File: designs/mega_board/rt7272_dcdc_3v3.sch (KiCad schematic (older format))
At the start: 14 parts, among them U2 RT7272

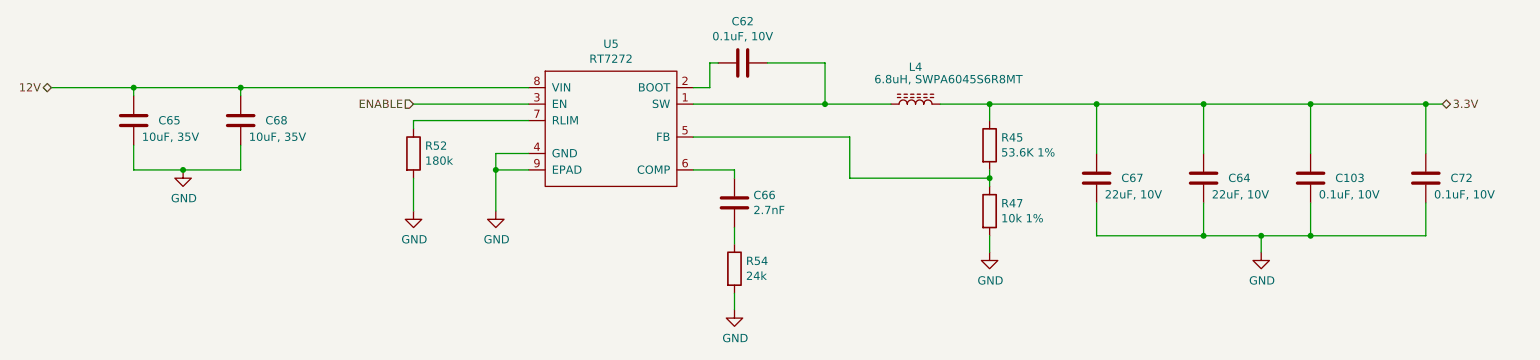
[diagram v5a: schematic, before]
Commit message: Add BOM definition to all resistors
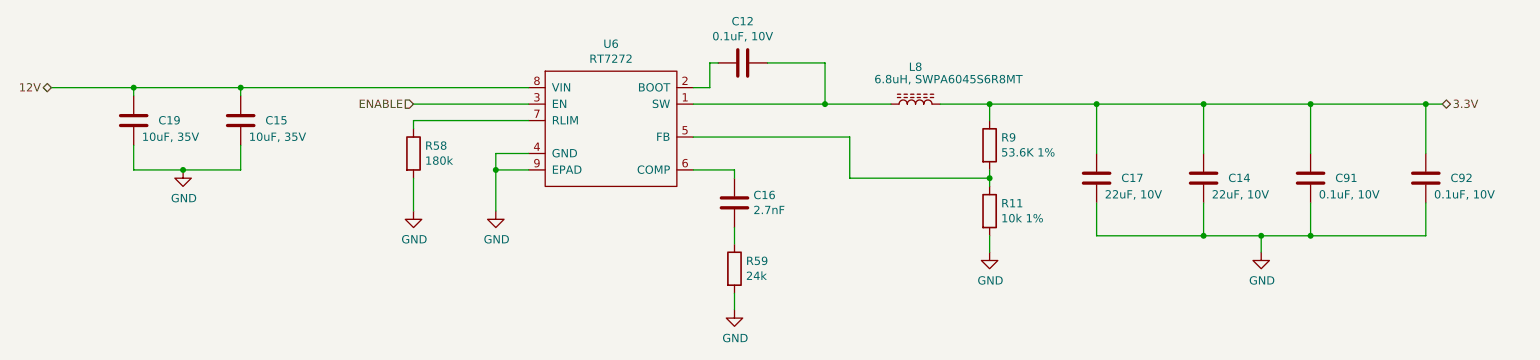
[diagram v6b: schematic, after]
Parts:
- R14: Manufacturer (none) -> Panasonic Electronic Components; Manufacturer PN (none) -> ERJ-2RKF5362X; Supplier (none) -> DigiKey; Supplier PN (none) -> P53.6KLDKR-ND
- R15: Manufacturer (none) -> Panasonic Electronic Components; Manufacturer PN (none) -> ERJ-PA2F1002X; Supplier (none) -> DigiKey; Supplier PN (none) -> P17230DKR-ND
- R19: Manufacturer (none) -> Panasonic Electronic Components; Manufacturer PN (none) -> ERJ-PA2F1803X; Supplier (none) -> DigiKey; Supplier PN (none) -> P124450DKR-ND
- R37: Manufacturer (none) -> Panasonic Electronic Components; Manufacturer PN (none) -> ERJ-PA2F2402X; Supplier (none) -> DigiKey; Supplier PN (none) -> P124459DKR-ND
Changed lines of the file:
@@
 $Descr A4 11693 8268
 encoding utf-8
-Sheet 5 14
+Sheet 6 14
 Title ""
 Date ""
@@
 AR Path="/5D0328DE/5D42E225/5D42D1B4" Ref="U6"  Part="1"
 AR Path="/5D42D1B4" Ref="U?"  Part="1"
-F 0 "U5" H 5600 4015 50  0000 C CNN
+F 0 "U6" H 5600 4015 50  0000 C CNN
 F 1 "RT7272" H 5600 3924 50  0000 C CNN
 F 2 "LibreRouter_MegaBoard:RT8250-SOP8" H 5600 3500 50  0001 C CNN
@@
 AR Path="/5D0328DE/5D42CD47/5D42D229" Ref="C29"  Part="1"
 AR Path="/5D0328DE/5D42E225/5D42D229" Ref="C15"  Part="1"
-F 0 "C68" H 3500 3450 50  0000 L CNN
+F 0 "C15" H 3500 3450 50  0000 L CNN
 F 1 "10uF, 35V" H 3400 3350 50  0000 L CNN
 F 2 "LibreRouter_MegaBoard:C0805" H 3388 3300 50  0001 C CNN
@@
 AR Path="/5D0328DE/5D42CD47/5D42D2DE" Ref="R19"  Part="1"
 AR Path="/5D0328DE/5D42E225/5D42D2DE" Ref="R58"  Part="1"
-F 0 "R52" H 4470 3696 50  0000 L CNN
+F 0 "R58" H 4470 3696 50  0000 L CNN
 F 1 "180k" H 4470 3605 50  0000 L CNN
 F 2 "LibreRouter_MegaBoard:R0402" V 4330 3650 50  0001 C CNN
 F 3 "~" H 4400 3650 50  0001 C CNN
+F 4 "Panasonic Electronic Components" H 4400 3650 50  0001 C CNN "Manufacturer"
+F 5 "ERJ-PA2F1803X" H 4400 3650 50  0001 C CNN "Manufacturer PN"
+F 6 "DigiKey" H 4400 3650 50  0001 C CNN "Supplier"
+F 7 "P124450DKR-ND" H 4400 3650 50  0001 C CNN "Supplier PN"
 	1    4400 3650
 	1    0    0    -1
@@
 AR Path="/5D0328DE/5D42CD47/5D42D3B9" Ref="L2"  Part="1"
 AR Path="/5D0328DE/5D42E225/5D42D3B9" Ref="L8"  Part="1"
-F 0 "L4" V 7675 3350 50  0000 C CNN
+F 0 "L8" V 7675 3350 50  0000 C CNN
 F 1 "6.8uH, SWPA6045S6R8MT" V 7600 3150 50  0000 C CNN
 F 2 "LibreRouter_MegaBoard:SWPA6028S" H 7450 3350 50  0001 C CNN
@@
 AR Path="/5D0328DE/5D42CD47/5D42D488" Ref="C13"  Part="1"
 AR Path="/5D0328DE/5D42E225/5D42D488" Ref="C12"  Part="1"
-F 0 "C62" V 6148 3100 50  0000 C CNN
+F 0 "C12" V 6148 3100 50  0000 C CNN
 F 1 "0.1uF, 10V" V 6239 3100 50  0000 C CNN
 F 2 "LibreRouter_MegaBoard:C0402" H 6438 2950 50  0001 C CNN
@@
 AR Path="/5D0328DE/5D42CD47/5D42D571" Ref="R14"  Part="1"
 AR Path="/5D0328DE/5D42E225/5D42D571" Ref="R9"  Part="1"
-F 0 "R45" H 7970 3646 50  0000 L CNN
+F 0 "R9" H 7970 3646 50  0000 L CNN
 F 1 "53.6K 1%" H 7970 3555 50  0000 L CNN
 F 2 "LibreRouter_MegaBoard:R0402" V 7830 3600 50  0001 C CNN
 F 3 "~" H 7900 3600 50  0001 C CNN
+F 4 "Panasonic Electronic Components" H 7900 3600 50  0001 C CNN "Manufacturer"
+F 5 "ERJ-2RKF5362X" H 7900 3600 50  0001 C CNN "Manufacturer PN"
+F 6 "DigiKey" H 7900 3600 50  0001 C CNN "Supplier"
+F 7 "P53.6KLDKR-ND" H 7900 3600 50  0001 C CNN "Supplier PN"
 	1    7900 3600
 	1    0    0    -1
@@
 AR Path="/5D0328DE/5D42CD47/5D42D5CB" Ref="R15"  Part="1"
 AR Path="/5D0328DE/5D42E225/5D42D5CB" Ref="R11"  Part="1"
-F 0 "R47" H 7970 4046 50  0000 L CNN
+F 0 "R11" H 7970 4046 50  0000 L CNN
 F 1 "10k 1%" H 7970 3955 50  0000 L CNN
 F 2 "LibreRouter_MegaBoard:R0402" V 7830 4000 50  0001 C CNN
 F 3 "~" H 7900 4000 50  0001 C CNN
+F 4 "Panasonic Electronic Components" H 7900 4000 50  0001 C CNN "Manufacturer"
+F 5 "ERJ-PA2F1002X" H 7900 4000 50  0001 C CNN "Manufacturer PN"
+F 6 "DigiKey" H 7900 4000 50  0001 C CNN "Supplier"
+F 7 "P17230DKR-ND" H 7900 4000 50  0001 C CNN "Supplier PN"
 	1    7900 4000
 	1    0    0    -1
@@
 AR Path="/5D0328DE/5D42CD47/5D42D605" Ref="R37"  Part="1"
 AR Path="/5D0328DE/5D42E225/5D42D605" Ref="R59"  Part="1"
-F 0 "R54" H 6420 4396 50  0000 L CNN
+F 0 "R59" H 6420 4396 50  0000 L CNN
 F 1 "24k" H 6420 4305 50  0000 L CNN
 F 2 "LibreRouter_MegaBoard:R0402" V 6280 4350 50  0001 C CNN
 F 3 "~" H 6350 4350 50  0001 C CNN
+F 4 "Panasonic Electronic Components" H 6350 4350 50  0001 C CNN "Manufacturer"
+F 5 "ERJ-PA2F2402X" H 6350 4350 50  0001 C CNN "Manufacturer PN"
+F 6 "DigiKey" H 6350 4350 50  0001 C CNN "Supplier"
+F 7 "P124459DKR-ND" H 6350 4350 50  0001 C CNN "Supplier PN"
 	1    6350 4350
 	1    0    0    -1
@@
 AR Path="/5D0328DE/5D42CD47/5D42D659" Ref="C32"  Part="1"
 AR Path="/5D0328DE/5D42E225/5D42D659" Ref="C16"  Part="1"
-F 0 "C66" H 6235 3904 50  0000 R CNN
+F 0 "C16" H 6235 3904 50  0000 R CNN
 F 1 "2.7nF" H 6235 3995 50  0000 R CNN
 F 2 "LibreRouter_MegaBoard:C0402" H 6388 3800 50  0001 C CNN
@@
 AR Path="/5D0328DE/5D42CD47/5D42DAC0" Ref="C38"  Part="1"
 AR Path="/5D0328DE/5D42E225/5D42DAC0" Ref="C17"  Part="1"
-F 0 "C67" H 8400 3800 50  0000 R CNN
+F 0 "C17" H 8400 3800 50  0000 R CNN
 F 1 "22uF, 10V" H 8500 3900 50  0000 R CNN
 F 2 "LibreRouter_MegaBoard:C0805" H 8588 3650 50  0001 C CNN
@@
 AR Path="/5D0328DE/5D42CD47/5D42DBCD" Ref="C28"  Part="1"
 AR Path="/5D0328DE/5D42E225/5D42DBCD" Ref="C14"  Part="1"
-F 0 "C64" H 9050 3800 50  0000 R CNN
+F 0 "C14" H 9050 3800 50  0000 R CNN
 F 1 "22uF, 10V" H 9150 3900 50  0000 R CNN
 F 2 "LibreRouter_MegaBoard:C0805" H 9238 3650 50  0001 C CNN
@@
 AR Path="/5D0328DE/5D42CD47/5D42DC2B" Ref="C71"  Part="1"
 AR Path="/5D0328DE/5D42E225/5D42DC2B" Ref="C91"  Part="1"
-F 0 "C103" H 9700 3800 50  0000 R CNN
+F 0 "C91" H 9700 3800 50  0000 R CNN
 F 1 "0.1uF, 10V" H 9800 3900 50  0000 R CNN
 F 2 "LibreRouter_MegaBoard:C0402" H 9888 3650 50  0001 C CNN
@@
 AR Path="/5D0328DE/5D42CD47/5D42DCB2" Ref="C72"  Part="1"
 AR Path="/5D0328DE/5D42E225/5D42DCB2" Ref="C92"  Part="1"
-F 0 "C72" H 10400 3800 50  0000 R CNN
+F 0 "C92" H 10400 3800 50  0000 R CNN
 F 1 "0.1uF, 10V" H 10500 3900 50  0000 R CNN
 F 2 "LibreRouter_MegaBoard:C0402" H 10588 3650 50  0001 C CNN
@@
 AR Path="/5D0328DE/5D42CD47/5D42DD90" Ref="#PWR0139"  Part="1"
 AR Path="/5D0328DE/5D42E225/5D42DD90" Ref="#PWR0145"  Part="1"
-F 0 "#PWR0139" H 7900 4000 50  0001 C CNN
+F 0 "#PWR0145" H 7900 4000 50  0001 C CNN
 F 1 "GND" H 7905 4077 50  0000 C CNN
 F 2 "" H 7900 4250 50  0001 C CNN
@@
 AR Path="/5D0328DE/5D42CD47/5D42DDBC" Ref="#PWR0140"  Part="1"
 AR Path="/5D0328DE/5D42E225/5D42DDBC" Ref="#PWR0146"  Part="1"
-F 0 "#PWR0140" H 9550 4000 50  0001 C CNN
+F 0 "#PWR0146" H 9550 4000 50  0001 C CNN
 F 1 "GND" H 9555 4077 50  0000 C CNN
 F 2 "" H 9550 4250 50  0001 C CNN
@@
 AR Path="/5D0328DE/5D42CD47/5D42FF27" Ref="#PWR0141"  Part="1"
 AR Path="/5D0328DE/5D42E225/5D42FF27" Ref="#PWR0147"  Part="1"
-F 0 "#PWR0141" H 6350 4350 50  0001 C CNN
+F 0 "#PWR0147" H 6350 4350 50  0001 C CNN
 F 1 "GND" H 6355 4427 50  0000 C CNN
 F 2 "" H 6350 4600 50  0001 C CNN
@@
 AR Path="/5D0328DE/5D42CD47/5D43058C" Ref="C36"  Part="1"
 AR Path="/5D0328DE/5D42E225/5D43058C" Ref="C19"  Part="1"
-F 0 "C65" H 2850 3450 50  0000 L CNN
+F 0 "C19" H 2850 3450 50  0000 L CNN
 F 1 "10uF, 35V" H 2750 3350 50  0000 L CNN
 F 2 "LibreRouter_MegaBoard:C0805" H 2738 3300 50  0001 C CNN
@@
 AR Path="/5D0328DE/5D42CD47/5D4322E2" Ref="#PWR0142"  Part="1"
 AR Path="/5D0328DE/5D42E225/5D4322E2" Ref="#PWR0148"  Part="1"
-F 0 "#PWR0142" H 3000 3500 50  0001 C CNN
+F 0 "#PWR0148" H 3000 3500 50  0001 C CNN
 F 1 "GND" H 3005 3577 50  0000 C CNN
 F 2 "" H 3000 3750 50  0001 C CNN
@@
 AR Path="/5D0328DE/5D42CD47/5D4323C5" Ref="#PWR0143"  Part="1"
 AR Path="/5D0328DE/5D42E225/5D4323C5" Ref="#PWR0149"  Part="1"
-F 0 "#PWR0143" H 4400 3750 50  0001 C CNN
+F 0 "#PWR0149" H 4400 3750 50  0001 C CNN
 F 1 "GND" H 4405 3827 50  0000 C CNN
 F 2 "" H 4400 4000 50  0001 C CNN
@@
 AR Path="/5D0328DE/5D42CD47/5D4323EC" Ref="#PWR0144"  Part="1"
 AR Path="/5D0328DE/5D42E225/5D4323EC" Ref="#PWR0150"  Part="1"
-F 0 "#PWR0144" H 4900 3750 50  0001 C CNN
+F 0 "#PWR0150" H 4900 3750 50  0001 C CNN
 F 1 "GND" H 4905 3827 50  0000 C CNN
 F 2 "" H 4900 4000 50  0001 C CNN

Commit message: Add BOM definition for components. We need more iformation for all the components that are not defined.
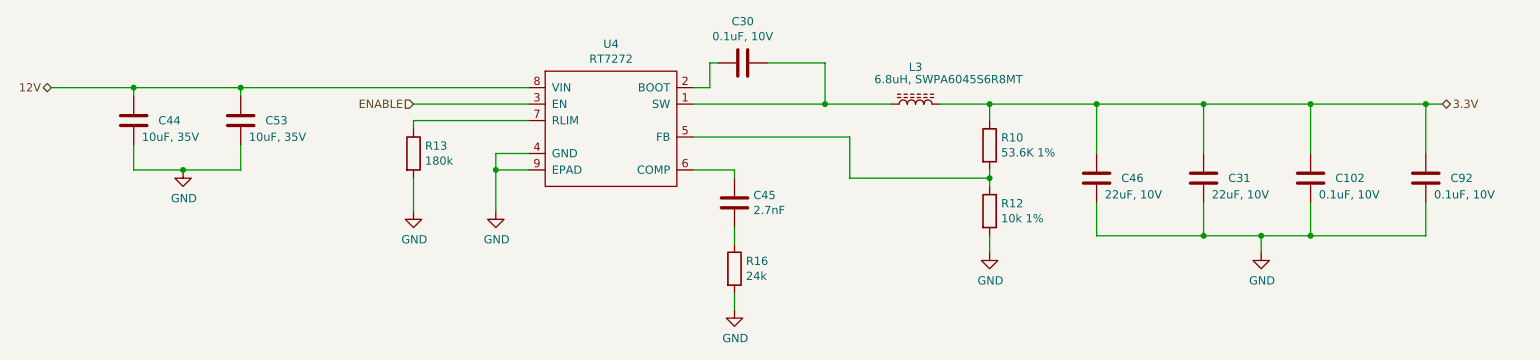
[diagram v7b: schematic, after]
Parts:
- L2: Manufacturer (none) -> Abracon LLC; Manufacturer PN (none) -> ASPI-6045S-6R8M-T; Supplier (none) -> DigiKey; Supplier PN (none) -> 535-13046-6-ND
- U2: Manufacturer (none) -> Richtek USA Inc.; Manufacturer PN (none) -> RT7272AGSP; Supplier (none) -> DigiKey; Supplier PN (none) -> RT7272AGSPDKR-ND
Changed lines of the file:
@@
 AR Path="/5D0328DE/5D42E225/5D42D1B4" Ref="U6"  Part="1"
 AR Path="/5D42D1B4" Ref="U?"  Part="1"
-F 0 "U6" H 5600 4015 50  0000 C CNN
+F 0 "U4" H 5600 4015 50  0000 C CNN
 F 1 "RT7272" H 5600 3924 50  0000 C CNN
 F 2 "LibreRouter_MegaBoard:RT8250-SOP8" H 5600 3500 50  0001 C CNN
 F 3 "" H 5600 3500 50  0001 C CNN
+F 4 "Richtek USA Inc." H 5600 3500 50  0001 C CNN "Manufacturer"
+F 5 "RT7272AGSP" H 5600 3500 50  0001 C CNN "Manufacturer PN"
+F 6 "DigiKey" H 5600 3500 50  0001 C CNN "Supplier"
+F 7 "RT7272AGSPDKR-ND" H 5600 3500 50  0001 C CNN "Supplier PN"
 	1    5600 3500
 	1    0    0    -1
@@
 AR Path="/5D0328DE/5D42CD47/5D42D229" Ref="C29"  Part="1"
 AR Path="/5D0328DE/5D42E225/5D42D229" Ref="C15"  Part="1"
-F 0 "C15" H 3500 3450 50  0000 L CNN
+F 0 "C53" H 3500 3450 50  0000 L CNN
 F 1 "10uF, 35V" H 3400 3350 50  0000 L CNN
 F 2 "LibreRouter_MegaBoard:C0805" H 3388 3300 50  0001 C CNN
@@
 AR Path="/5D0328DE/5D42CD47/5D42D2DE" Ref="R19"  Part="1"
 AR Path="/5D0328DE/5D42E225/5D42D2DE" Ref="R58"  Part="1"
-F 0 "R58" H 4470 3696 50  0000 L CNN
+F 0 "R13" H 4470 3696 50  0000 L CNN
 F 1 "180k" H 4470 3605 50  0000 L CNN
 F 2 "LibreRouter_MegaBoard:R0402" V 4330 3650 50  0001 C CNN
@@
 AR Path="/5D0328DE/5D42CD47/5D42D3B9" Ref="L2"  Part="1"
 AR Path="/5D0328DE/5D42E225/5D42D3B9" Ref="L8"  Part="1"
-F 0 "L8" V 7675 3350 50  0000 C CNN
+F 0 "L3" V 7675 3350 50  0000 C CNN
 F 1 "6.8uH, SWPA6045S6R8MT" V 7600 3150 50  0000 C CNN
 F 2 "LibreRouter_MegaBoard:SWPA6028S" H 7450 3350 50  0001 C CNN
 F 3 "~" H 7450 3350 50  0001 C CNN
+F 4 "Abracon LLC" H 7450 3350 50  0001 C CNN "Manufacturer"
+F 5 "ASPI-6045S-6R8M-T" H 7450 3350 50  0001 C CNN "Manufacturer PN"
+F 6 "DigiKey" H 7450 3350 50  0001 C CNN "Supplier"
+F 7 "535-13046-6-ND" H 7450 3350 50  0001 C CNN "Supplier PN"
 	1    7450 3350
 	0    -1   -1   0
@@
 AR Path="/5D0328DE/5D42CD47/5D42D488" Ref="C13"  Part="1"
 AR Path="/5D0328DE/5D42E225/5D42D488" Ref="C12"  Part="1"
-F 0 "C12" V 6148 3100 50  0000 C CNN
+F 0 "C30" V 6148 3100 50  0000 C CNN
 F 1 "0.1uF, 10V" V 6239 3100 50  0000 C CNN
 F 2 "LibreRouter_MegaBoard:C0402" H 6438 2950 50  0001 C CNN
@@
 AR Path="/5D0328DE/5D42CD47/5D42D571" Ref="R14"  Part="1"
 AR Path="/5D0328DE/5D42E225/5D42D571" Ref="R9"  Part="1"
-F 0 "R9" H 7970 3646 50  0000 L CNN
+F 0 "R10" H 7970 3646 50  0000 L CNN
 F 1 "53.6K 1%" H 7970 3555 50  0000 L CNN
 F 2 "LibreRouter_MegaBoard:R0402" V 7830 3600 50  0001 C CNN
@@
 AR Path="/5D0328DE/5D42CD47/5D42D5CB" Ref="R15"  Part="1"
 AR Path="/5D0328DE/5D42E225/5D42D5CB" Ref="R11"  Part="1"
-F 0 "R11" H 7970 4046 50  0000 L CNN
+F 0 "R12" H 7970 4046 50  0000 L CNN
 F 1 "10k 1%" H 7970 3955 50  0000 L CNN
 F 2 "LibreRouter_MegaBoard:R0402" V 7830 4000 50  0001 C CNN
@@
 AR Path="/5D0328DE/5D42CD47/5D42D605" Ref="R37"  Part="1"
 AR Path="/5D0328DE/5D42E225/5D42D605" Ref="R59"  Part="1"
-F 0 "R59" H 6420 4396 50  0000 L CNN
+F 0 "R16" H 6420 4396 50  0000 L CNN
 F 1 "24k" H 6420 4305 50  0000 L CNN
 F 2 "LibreRouter_MegaBoard:R0402" V 6280 4350 50  0001 C CNN
@@
 AR Path="/5D0328DE/5D42CD47/5D42D659" Ref="C32"  Part="1"
 AR Path="/5D0328DE/5D42E225/5D42D659" Ref="C16"  Part="1"
-F 0 "C16" H 6235 3904 50  0000 R CNN
+F 0 "C45" H 6235 3904 50  0000 R CNN
 F 1 "2.7nF" H 6235 3995 50  0000 R CNN
 F 2 "LibreRouter_MegaBoard:C0402" H 6388 3800 50  0001 C CNN
@@
 AR Path="/5D0328DE/5D42CD47/5D42DAC0" Ref="C38"  Part="1"
 AR Path="/5D0328DE/5D42E225/5D42DAC0" Ref="C17"  Part="1"
-F 0 "C17" H 8400 3800 50  0000 R CNN
+F 0 "C46" H 8400 3800 50  0000 R CNN
 F 1 "22uF, 10V" H 8500 3900 50  0000 R CNN
 F 2 "LibreRouter_MegaBoard:C0805" H 8588 3650 50  0001 C CNN
@@
 AR Path="/5D0328DE/5D42CD47/5D42DBCD" Ref="C28"  Part="1"
 AR Path="/5D0328DE/5D42E225/5D42DBCD" Ref="C14"  Part="1"
-F 0 "C14" H 9050 3800 50  0000 R CNN
+F 0 "C31" H 9050 3800 50  0000 R CNN
 F 1 "22uF, 10V" H 9150 3900 50  0000 R CNN
 F 2 "LibreRouter_MegaBoard:C0805" H 9238 3650 50  0001 C CNN
@@
 AR Path="/5D0328DE/5D42CD47/5D42DC2B" Ref="C71"  Part="1"
 AR Path="/5D0328DE/5D42E225/5D42DC2B" Ref="C91"  Part="1"
-F 0 "C91" H 9700 3800 50  0000 R CNN
+F 0 "C102" H 9700 3800 50  0000 R CNN
 F 1 "0.1uF, 10V" H 9800 3900 50  0000 R CNN
 F 2 "LibreRouter_MegaBoard:C0402" H 9888 3650 50  0001 C CNN
@@
 AR Path="/5D0328DE/5D42CD47/5D43058C" Ref="C36"  Part="1"
 AR Path="/5D0328DE/5D42E225/5D43058C" Ref="C19"  Part="1"
-F 0 "C19" H 2850 3450 50  0000 L CNN
+F 0 "C44" H 2850 3450 50  0000 L CNN
 F 1 "10uF, 35V" H 2750 3350 50  0000 L CNN
 F 2 "LibreRouter_MegaBoard:C0805" H 2738 3300 50  0001 C CNN
